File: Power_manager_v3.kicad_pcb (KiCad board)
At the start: 4 copper layers, 80 parts, among them J1 L_input, J2 Pow_mng_pow, J3 Load1, J4 Load2, J5 SWD (PLS5), J6 Dig_mod_iface, Q1 2N5551S, Q2 2N5551S, U1 DC12003, U2 G3MB-202PL, U3 G3MB-202PL, U4 DC5V_DC5V3V3_v3, U5 STM32F030F4Px, U6 HLW8112, U7 ADuM_I2C_v3, Y1 CSTCE8M, Y2 ABLS-3.579545MHZ-D-3-Y-T

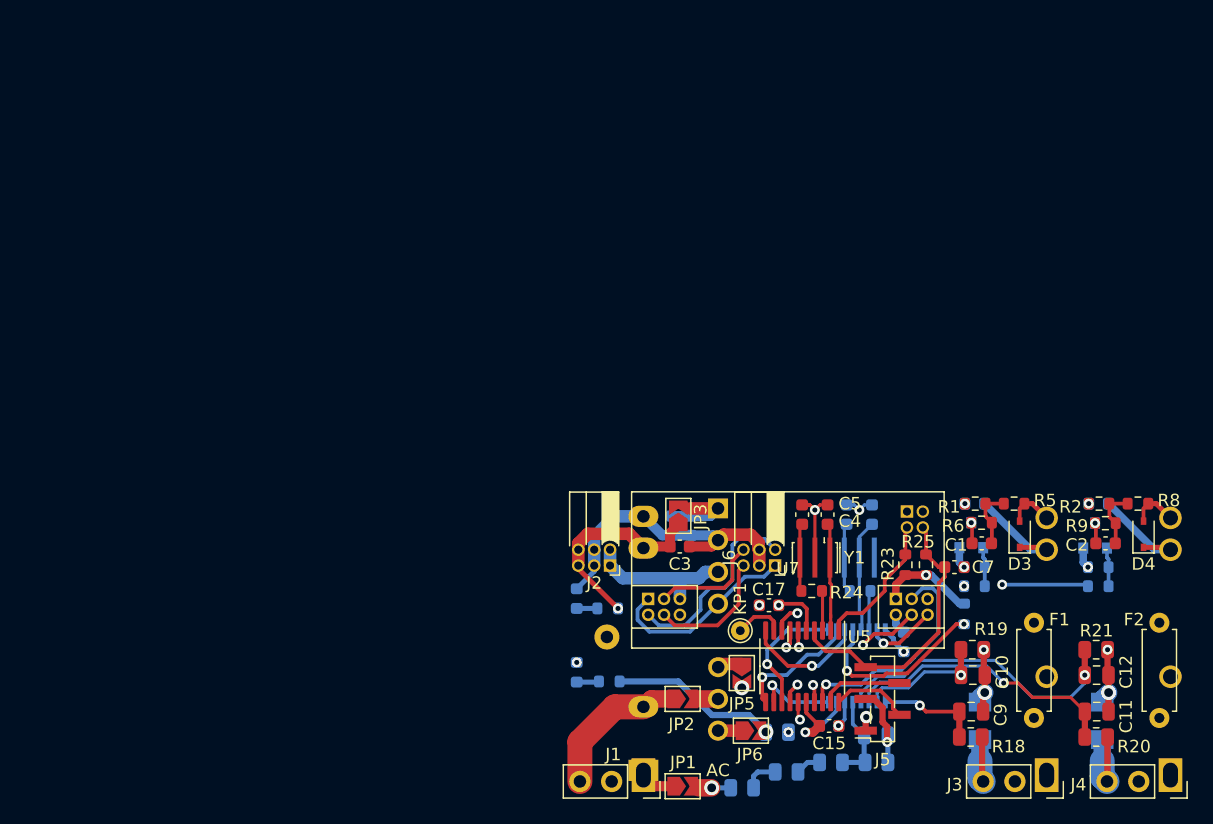
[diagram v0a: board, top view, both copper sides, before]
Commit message: Сформирован перечень элементов, 3D-модель, исправлены ошибки, реализована панелизация платы.
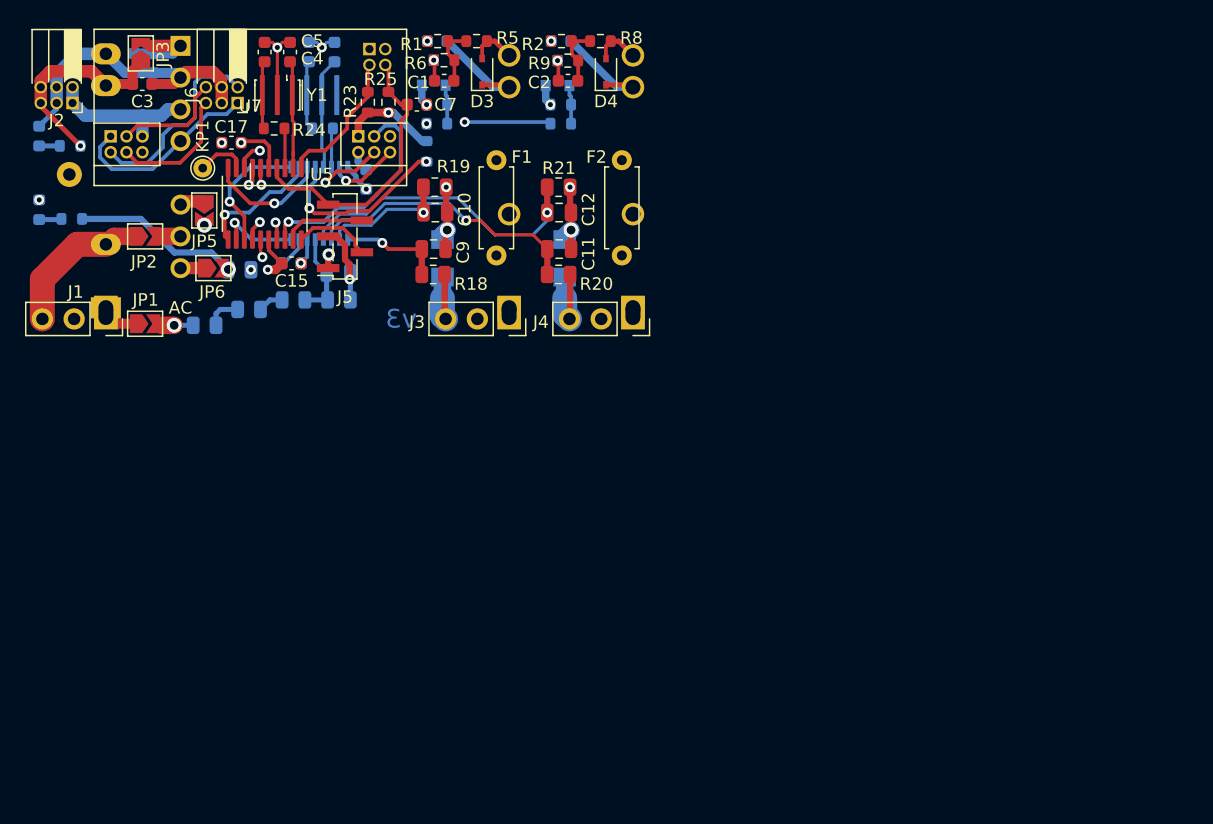
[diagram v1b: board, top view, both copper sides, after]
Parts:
- moved J3 56.7 mm to (85.7, 69.7)
- moved J4 56.7 mm to (95.6, 69.7)
- moved Q2 56.7 mm to (89.6, 50.1)
- moved U2 56.7 mm to (85.7, 69.0)
- moved U3 56.7 mm to (95.6, 69.0)
- moved C17 56.7 mm to (63.5, 55.6)
- moved C18 56.7 mm to (71.7, 48.4)
- moved C19 56.7 mm to (69.7, 48.4)
- moved C4 56.7 mm to (68.2, 48.4)
- moved C5 56.7 mm to (66.2, 48.4)
- moved GND1 56.7 mm to (50.5, 58.2)
- moved JP1 56.7 mm to (56.6, 70.1)
- moved JP4 56.7 mm to (74.5, 48.1)
- moved R12 56.7 mm to (61.4, 70.2)
- moved U7 56.7 mm to (65.0, 59.1)
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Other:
- board text added: "v3"
